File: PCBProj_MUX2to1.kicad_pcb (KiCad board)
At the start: 2 copper layers, 100 x 100 mm, 34 parts, among them J1 GS3, J2 GS3, J3 GS3, J4 GS3, J5 Socket_2mm, J6 Socket_2mm, U1 74HC00, U2 74HC00, X1 Conn_Coaxial, X2 Conn_Coaxial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

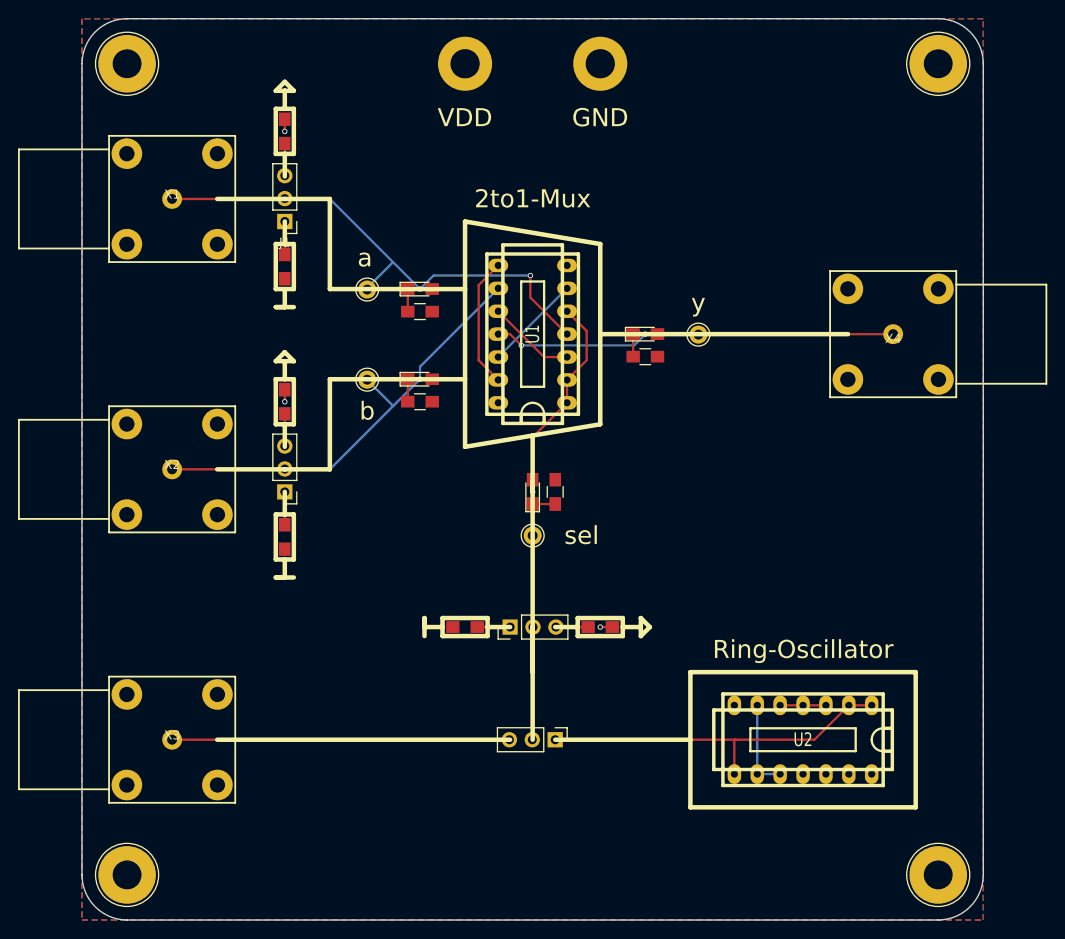
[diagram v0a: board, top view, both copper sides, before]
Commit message: Added holes for GND probes
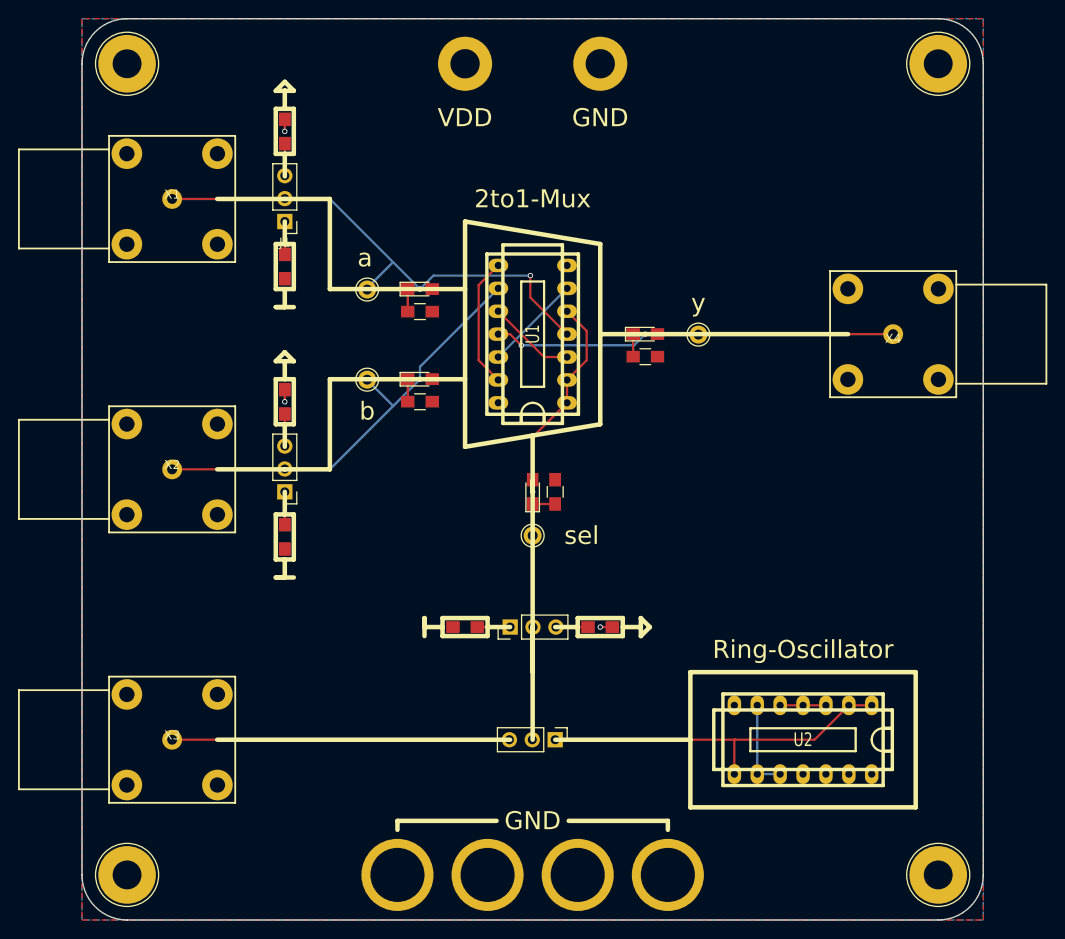
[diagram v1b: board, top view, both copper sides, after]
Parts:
- added J10: Hole, Mounting_Holes:MountingHole_6mm_Pad, F.Cu at (151.4, 134.7)
- added J7: Hole, Mounting_Holes:MountingHole_6mm_Pad, F.Cu at (121.4, 134.7)
- added J8: Hole, Mounting_Holes:MountingHole_6mm_Pad, F.Cu at (131.4, 134.7)
- added J9: Hole, Mounting_Holes:MountingHole_6mm_Pad, F.Cu at (141.4, 134.7)
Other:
- board text added: "PCBProj_MUX2to1 06.01.2018 - Rev. A"
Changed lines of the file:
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@@
 (kicad_pcb (version 4) (host pcbnew 4.0.7)
   (general
-    (links 70)
+    (links 74)
     (no_connects 0)
     (area 86.284999 39.624999 186.435001 139.775001)
     (thickness 1.6)
-    (drawings 105)
+    (drawings 111)
     (tracks 93)
     (zones 0)
-    (modules 34)
+    (modules 38)
     (nets 25)
   )
@@
     (45 Margin user hide)
     (46 B.CrtYd user)
-    (47 F.CrtYd user)
+    (47 F.CrtYd user hide)
     (48 B.Fab user)
     (49 F.Fab user)
@@
     (trace_clearance 0.2)
     (zone_clearance 0.4)
-    (zone_45_only no)
+    (zone_45_only yes)
     (trace_min 0.2)
     (segment_width 0.5)
@@
     (mod_text_size 1 1)
     (mod_text_width 0.15)
-    (pad_size 2 2)
-    (pad_drill 1.1)
+    (pad_size 8 8)
+    (pad_drill 6)
     (pad_to_mask_clearance 0.2)
     (aux_axis_origin 86.36 139.7)
@@
       (rotate (xyz 0 0 0))
     )
+  )
+  (module Mounting_Holes:MountingHole_6mm_Pad (layer F.Cu)
+    (at 121.36 134.7)
+    (descr "Mounting Hole 6mm")
+    (tags "mounting hole 6mm")
+    (attr virtual)
+    (fp_text reference J7 (at 0 -7) (layer F.SilkS) hide
+      (effects (font (size 1 1) (thickness 0.15)))
+    )
+    (fp_text value Hole (at 0 2) (layer F.Fab) hide
+      (effects (font (size 1 1) (thickness 0.15)))
+    )
+    (fp_text user %R (at 0.3 0) (layer F.Fab)
+      (effects (font (size 1 1) (thickness 0.15)))
+    )
+    (fp_circle (center 0 0) (end 6 0) (layer Cmts.User) (width 0.15))
+    (fp_circle (center 0 0) (end 6.25 0) (layer F.CrtYd) (width 0.05))
+    (pad 1 thru_hole circle (at 0 0) (size 8 8) (drill 6) (layers *.Cu *.Mask)
+      (net 5 GND))
+  )
+  (module Mounting_Holes:MountingHole_6mm_Pad (layer F.Cu)
+    (at 131.36 134.7)
+    (descr "Mounting Hole 6mm")
+    (tags "mounting hole 6mm")
+    (attr virtual)
+    (fp_text reference J8 (at 0 -7) (layer F.SilkS) hide
+      (effects (font (size 1 1) (thickness 0.15)))
+    )
+    (fp_text value Hole (at 0 2) (layer F.Fab) hide
+      (effects (font (size 1 1) (thickness 0.15)))
+    )
+    (fp_text user %R (at 0.3 0) (layer F.Fab)
+      (effects (font (size 1 1) (thickness 0.15)))
+    )
+    (fp_circle (center 0 0) (end 6 0) (layer Cmts.User) (width 0.15))
+    (fp_circle (center 0 0) (end 6.25 0) (layer F.CrtYd) (width 0.05))
+    (pad 1 thru_hole circle (at 0 0) (size 8 8) (drill 6) (layers *.Cu *.Mask)
+      (net 5 GND))
+  )
+  (module Mounting_Holes:MountingHole_6mm_Pad (layer F.Cu)
+    (at 141.36 134.7)
+    (descr "Mounting Hole 6mm")
+    (tags "mounting hole 6mm")
+    (attr virtual)
+    (fp_text reference J9 (at 0 -7) (layer F.SilkS) hide
+      (effects (font (size 1 1) (thickness 0.15)))
+    )
+    (fp_text value Hole (at 0 2) (layer F.Fab) hide
+      (effects (font (size 1 1) (thickness 0.15)))
+    )
+    (fp_text user %R (at 0.3 0) (layer F.Fab)
+      (effects (font (size 1 1) (thickness 0.15)))
+    )
+    (fp_circle (center 0 0) (end 6 0) (layer Cmts.User) (width 0.15))
+    (fp_circle (center 0 0) (end 6.25 0) (layer F.CrtYd) (width 0.05))
+    (pad 1 thru_hole circle (at 0 0) (size 8 8) (drill 6) (layers *.Cu *.Mask)
+      (net 5 GND))
+  )
+  (module Mounting_Holes:MountingHole_6mm_Pad (layer F.Cu)
+    (at 151.36 134.7)
+    (descr "Mounting Hole 6mm")
+    (tags "mounting hole 6mm")
+    (attr virtual)
+    (fp_text reference J10 (at 0 -7) (layer F.SilkS) hide
+      (effects (font (size 1 1) (thickness 0.15)))
+    )
+    (fp_text value Hole (at 0 2) (layer F.Fab) hide
+      (effects (font (size 1 1) (thickness 0.15)))
+    )
+    (fp_text user %R (at 0.3 0) (layer F.Fab)
+      (effects (font (size 1 1) (thickness 0.15)))
+    )
+    (fp_circle (center 0 0) (end 6 0) (layer Cmts.User) (width 0.15))
+    (fp_circle (center 0 0) (end 6.25 0) (layer F.CrtYd) (width 0.05))
+    (pad 1 thru_hole circle (at 0 0) (size 8 8) (drill 6) (layers *.Cu *.Mask)
+      (net 5 GND))
+  )
+  (gr_text "PCBProj_MUX2to1\n06.01.2018 - Rev. A" (at 168.36 101.7) (layer B.SilkS)
+    (effects (font (size 1.5 1.5) (thickness 0.3)) (justify mirror))
+  )
+  (gr_line (start 121.36 128.7) (end 121.36 129.7) (angle 90) (layer F.SilkS) (width 0.5))
+  (gr_line (start 132.36 128.7) (end 121.36 128.7) (angle 90) (layer F.SilkS) (width 0.5))
+  (gr_line (start 151.36 128.7) (end 151.36 129.7) (angle 90) (layer F.SilkS) (width 0.5))
+  (gr_line (start 140.36 128.7) (end 151.36 128.7) (angle 90) (layer F.SilkS) (width 0.5))
+  (gr_text "GND\n" (at 136.36 128.7) (layer F.SilkS)
+    (effects (font (size 2 2) (thickness 0.3)))
   )
   (gr_line (start 86.36 44.7) (end 86.36 134.7) (angle 90) (layer Edge.Cuts) (width 0.15))
@@
     (polygon
       (pts
-        (xy 86.36 139.7) (xy 186.36 139.7) (xy 186.36 39.7) (xy 86.36 39.7)
+        (xy 186.36 139.7) (xy 86.36 139.7) (xy 86.36 39.7) (xy 186.36 39.7)
       )
     )
+  )
+  (zone (net 0) (net_name "") (layer B.Cu) (hatch edge 0.508)
+    (connect_pads (clearance 0.4))
+    (min_thickness 0.254)
+    (keepout (tracks not_allowed) (vias not_allowed) (copperpour not_allowed))
+    (fill (arc_segments 16) (thermal_gap 0.508) (thermal_bridge_width 0.508))
+    (polygon
+      (pts
+        (xy 116.36 139.7) (xy 116.36 132.2) (xy 118.86 129.7) (xy 153.86 129.7) (xy 156.36 132.2)
+        (xy 156.36 139.7)
+      )
+    )
